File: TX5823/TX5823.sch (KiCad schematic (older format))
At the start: 73 parts, among them IC1 ATMEGA328P-A, IC2 ATTINY13A-SS, P1 Akku_in, P2 ISP, P3 Mavlink, Q3 MOSFET_N, SW1 SW_PUSH, SW2 SW_PUSH, U2 TPS54531, U3 TPS7A7200RGT, U4 CONN_03X08, U5 OPTO-TRANSISTOR4, U6 TX5823, U7 MAX7456_DS, U8 OPTO-TRANSISTOR4, X1 27MHz, Y1 16MHz

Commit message: an Layout gearbeitet
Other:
- note added: "Achtung, 5V nicht anschließen"
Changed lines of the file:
@@
 	9550 1500 9600 1500
 Connection ~ 9600 1100
+Text Notes 14500 8400 0    60   ~ 0
+Achtung, 5V nicht anschließen
 $EndSCHEMATC

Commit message: Layout fertig bis auf startup teil
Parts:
- D1: footprint (none) -> toni:POWERDI5
- U7: footprint toni:TSSOP-20_4.4x6.5mm_Pitch0.65mm_EP -> toni:TSSOP-28_4.4x9.7mm_Pitch0.65mm_EP
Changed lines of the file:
@@
 F 0 "U7" H 14400 6600 60  0000 C CNN
 F 1 "MAX7456_DS" H 14000 8050 60  0000 C CNN
-F 2 "toni:TSSOP-20_4.4x6.5mm_Pitch0.65mm_EP" H 13850 7200 60  0001 C CNN
+F 2 "toni:TSSOP-28_4.4x9.7mm_Pitch0.65mm_EP" H 13850 7200 60  0001 C CNN
 F 3 "" H 13850 7200 60  0000 C CNN
 	1    13850 7200
@@
 F 0 "D1" H 4500 8650 40  0000 C CNN
 F 1 "DIODE" H 4500 8450 40  0000 C CNN
-F 2 "" H 4500 8550 60  0001 C CNN
+F 2 "toni:POWERDI5" H 4500 8550 60  0001 C CNN
 F 3 "" H 4500 8550 60  0001 C CNN
 F 4 "PDS760-13" H 4500 8550 60  0001 C CNN "Teilenummer"

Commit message: zusätzlicher LDO für OSD hinzugefügt Softstart hinzugefügt
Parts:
- added C10: 220pF, Capacitors_SMD:C_0402, symbol C
- added C12, C4: 1uF, Capacitors_SMD:C_0603, symbol C
- added C13: 10uF, Capacitors_SMD:C_1206, symbol C
- added C6, C7: 100nF, Capacitors_SMD:C_0402, symbol C
- added C9: C, Capacitors_SMD:C_0603, symbol C
- added D2: ZENER, Diodes_SMD:Diode-MiniMELF_Standard, symbol ZENER
- added Q1: MOSFET_P, toni:SO8_WITH_EP, symbol MOSFET_P
- added R1, R2: R, Resistors_SMD:R_0603, symbol R
- added R3: R, Resistors_SMD:R_1206, symbol R
- added R4: 280k, Resistors_SMD:R_0603, symbol R
- added R5: 30,9k, Resistors_SMD:R_0603, symbol R
- added U1: TPS7A7200RGT, toni:QFN-16-1EP_3x3mm_Pitch0.5mm, symbol TPS7A7200RGT
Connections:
- net +5V: now also C10.1, C12.1, C13.1, R4.1, U1.15 (OUT), U1.16 (OUT); no longer C16.1, C17.1, C19.1, C21.1, L1.2, R10.1, R14.1, R25.1, U3.12 (EN), U3.13 (IN), U3.14 (IN), U4.14 (5_2), U4.17 (6_2)
- net Akku+: now also Q1.D, R3.1; no longer C1.1, C3.1, U2.2 (VIN)
- net GND: now also C12.2, C13.2, C4.2, C6.2, C7.2, R1.2, R5.2, U1.17 (EP), U1.7 (GND)
- new net: C7.1, U1.11 (SS)
- new net: C10.2, R4.2, R5.1, U1.2 (FB)
- new net: C9.1, D2.2 (K), Q1.G, R1.1, R2.1
- new net 5,2V: C16.1, C17.1, C19.1, C21.1, C4.1, C6.1, L1.2, R10.1, R14.1, R25.1, U1.12 (EN), U1.13 (IN), U1.14 (IN), U3.12 (EN), U3.13 (IN), U3.14 (IN), U4.14 (5_2), U4.17 (6_2)
- new net Akku+_SS: C1.1, C3.1, C9.2, D2.1 (A), Q1.S, R2.2, R3.2, U2.2 (VIN)
- no-connect marks 27 -> 35
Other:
- note added: "Softstart"
- note added: "TODO:\n12V Aufsteckplatine\nEingangsschutz"
- note removed: "TODO:\nEingangsfilterung (spule und diode)\n12V Aufsteckplatine"
- moved on the sheet: P1, P3, R26, R27, R28, SW2, U8

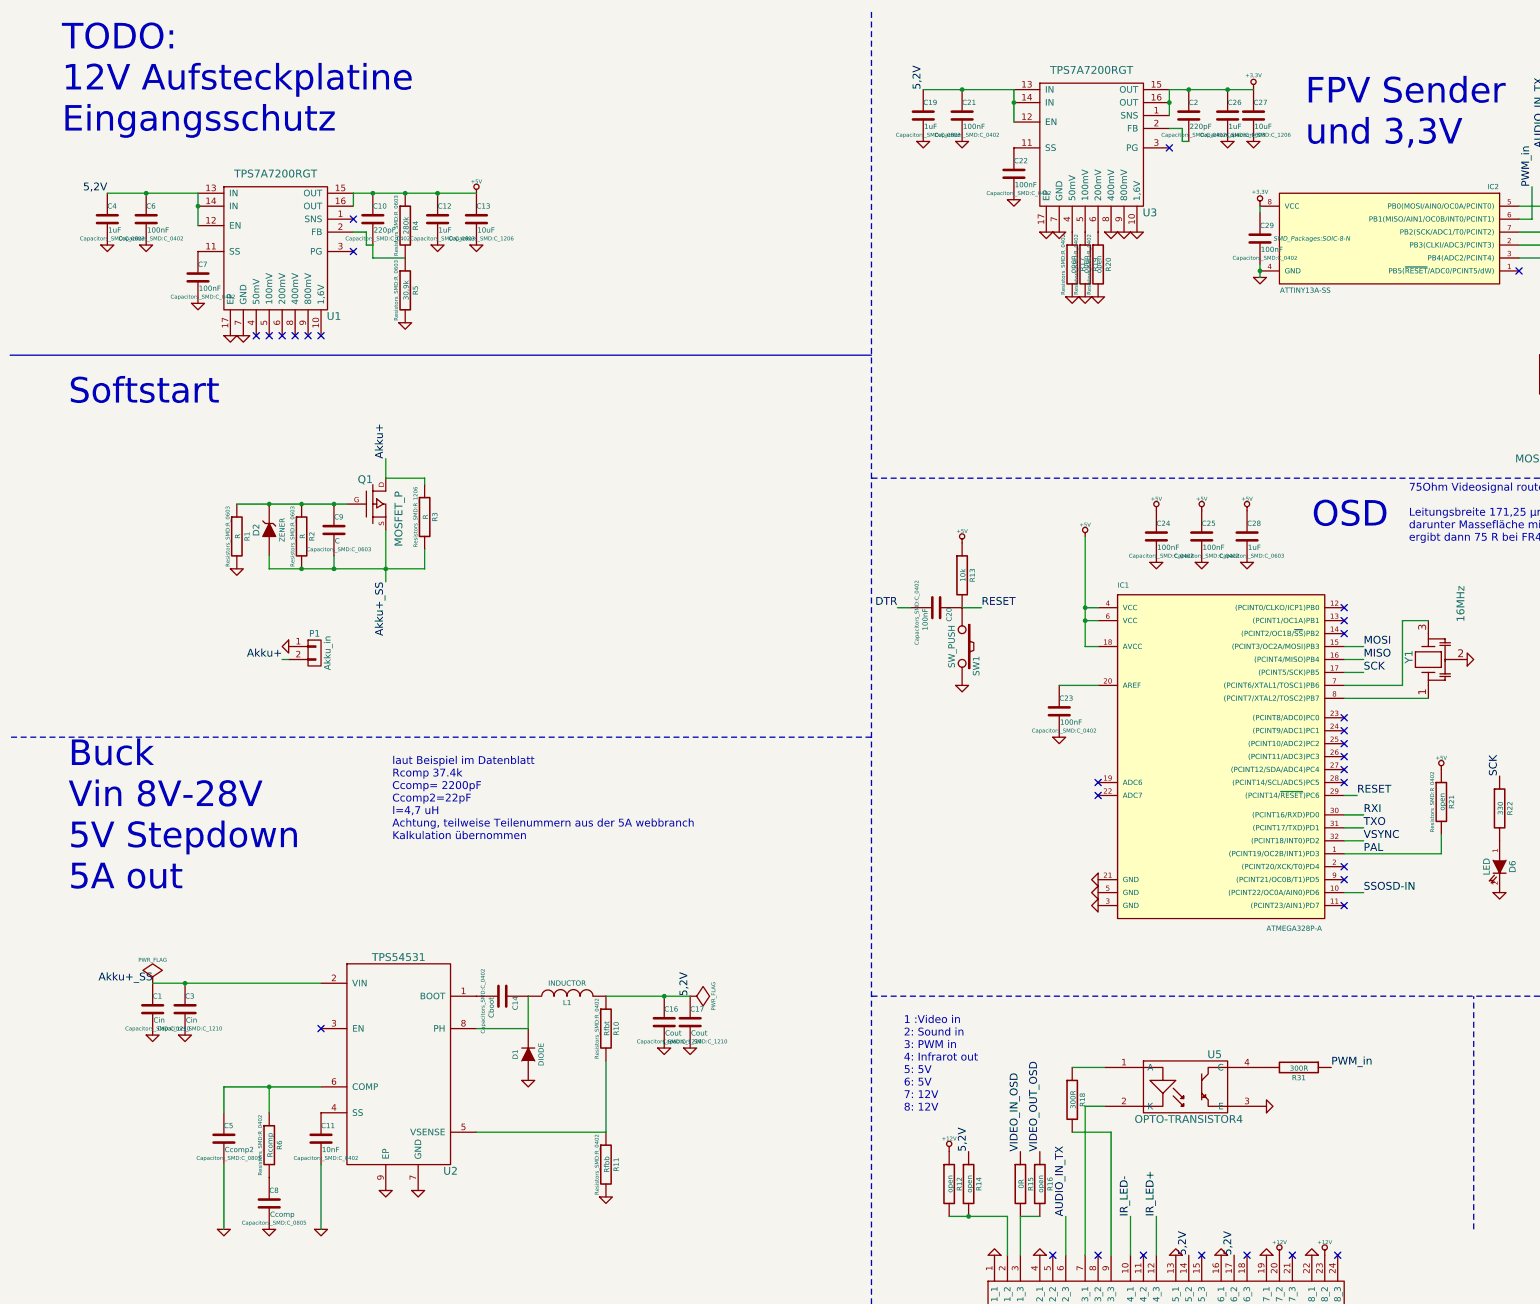
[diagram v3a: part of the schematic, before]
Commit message: Verbindungspunkte für 12V BuckBoost Aufsteckplatine hinzugefügt
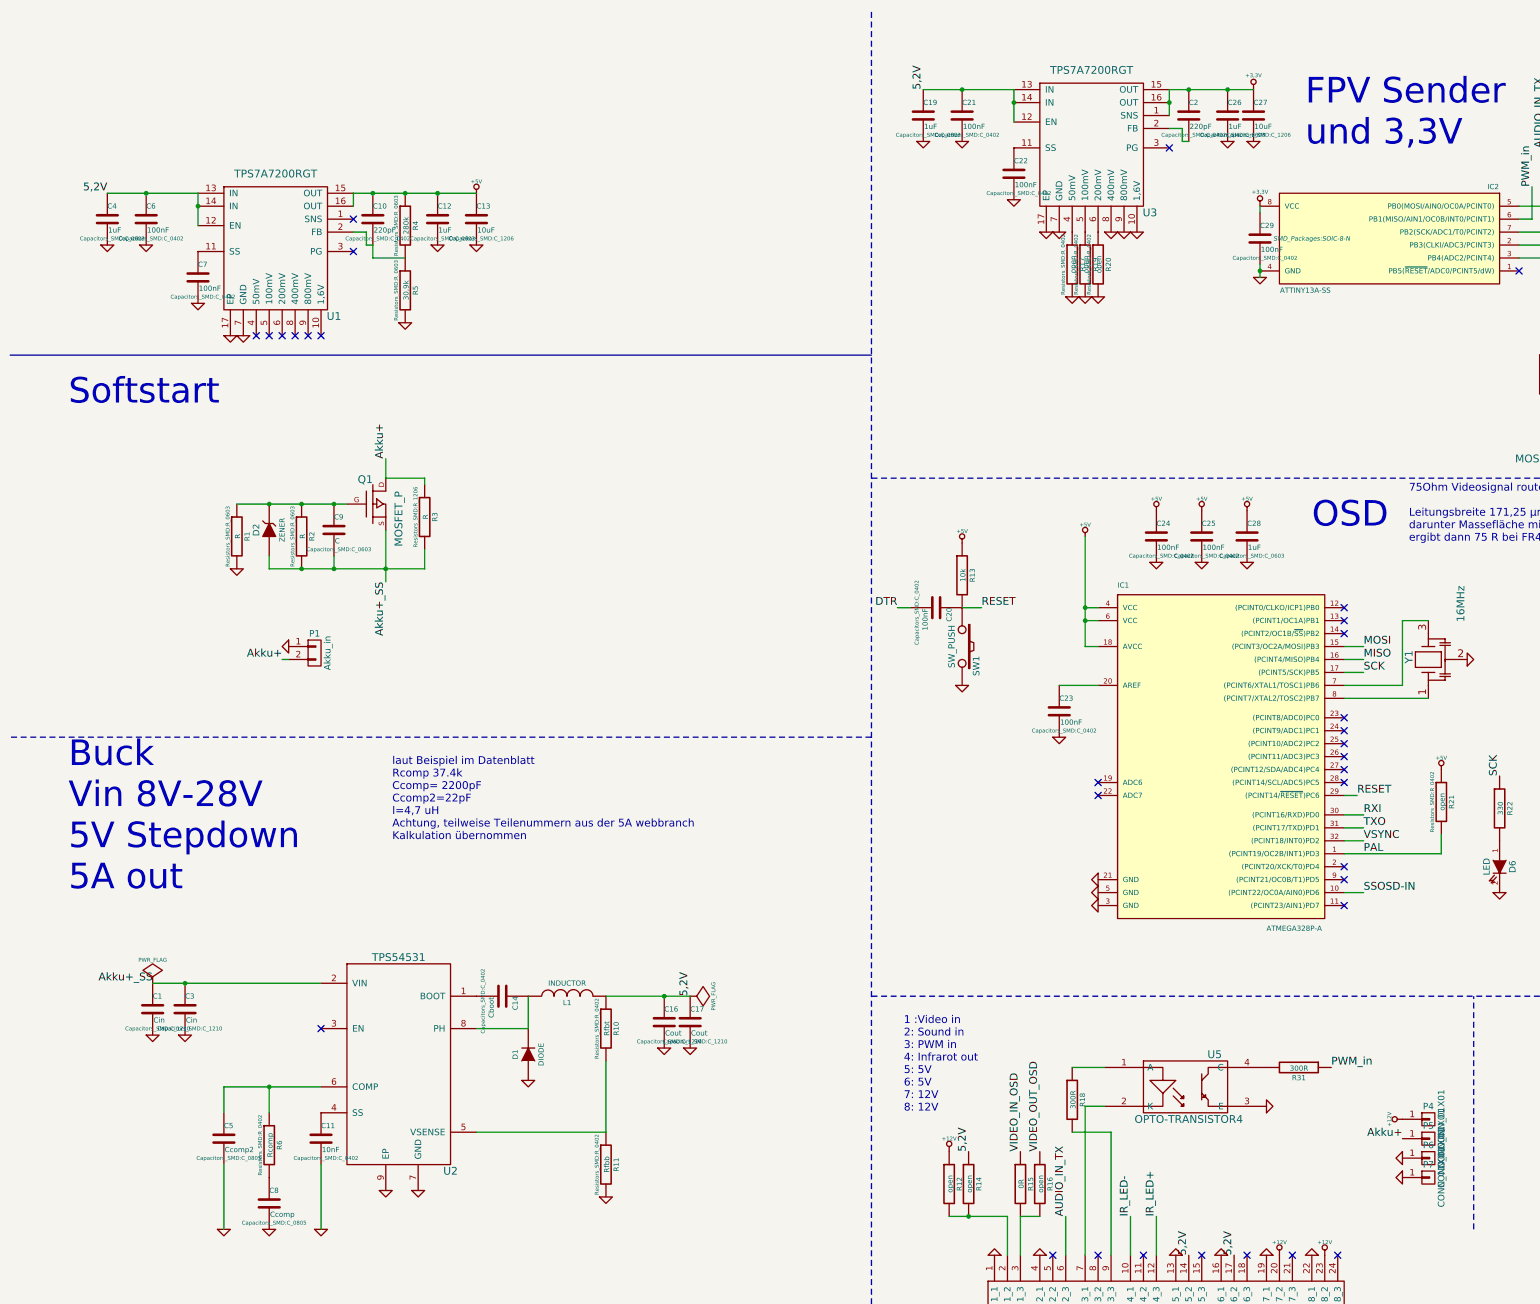
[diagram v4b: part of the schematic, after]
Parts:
- added P4, P5, P6, P7: CONN_01X01, Pin_Headers:Pin_Header_Straight_1x01, symbol CONN_01X01
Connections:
- net +12V: now also P4.1 (P1)
- net Akku+: now also P5.1 (P1)
- net GND: now also P6.1 (P1), P7.1 (P1)
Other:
- note removed: "TODO:\n12V Aufsteckplatine\nEingangsschutz"
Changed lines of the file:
@@
 	0    1    1    0
 $EndComp
-Text Notes 900  1450 0    197  ~ 0
-TODO:\n12V Aufsteckplatine\nEingangsschutz
 NoConn ~ 15300 5100
 NoConn ~ 15300 4700
@@
 Text Notes 950  3550 0    197  ~ 0
 Softstart
+$Comp
+L CONN_01X01 P4
+U 1 1 551FB334
+P 11450 9050
+F 0 "P4" H 11450 9150 50  0000 C CNN
+F 1 "CONN_01X01" V 11550 9050 50  0000 C CNN
+F 2 "Pin_Headers:Pin_Header_Straight_1x01" H 11450 9050 60  0001 C CNN
+F 3 "" H 11450 9050 60  0000 C CNN
+	1    11450 9050
+	1    0    0    -1
+$EndComp
+$Comp
+L CONN_01X01 P5
+U 1 1 551FB3E2
+P 11450 9200
+F 0 "P5" H 11450 9300 50  0000 C CNN
+F 1 "CONN_01X01" V 11550 9200 50  0000 C CNN
+F 2 "Pin_Headers:Pin_Header_Straight_1x01" H 11450 9200 60  0001 C CNN
+F 3 "" H 11450 9200 60  0000 C CNN
+	1    11450 9200
+	1    0    0    -1
+$EndComp
+$Comp
+L CONN_01X01 P6
+U 1 1 551FB45A
+P 11450 9350
+F 0 "P6" H 11450 9450 50  0000 C CNN
+F 1 "CONN_01X01" V 11550 9350 50  0000 C CNN
+F 2 "Pin_Headers:Pin_Header_Straight_1x01" H 11450 9350 60  0001 C CNN
+F 3 "" H 11450 9350 60  0000 C CNN
+	1    11450 9350
+	1    0    0    -1
+$EndComp
+$Comp
+L CONN_01X01 P7
+U 1 1 551FB4CB
+P 11450 9500
+F 0 "P7" H 11450 9600 50  0000 C CNN
+F 1 "CONN_01X01" V 11550 9500 50  0000 C CNN
+F 2 "Pin_Headers:Pin_Header_Straight_1x01" H 11450 9500 60  0001 C CNN
+F 3 "" H 11450 9500 60  0000 C CNN
+	1    11450 9500
+	1    0    0    -1
+$EndComp
+$Comp
+L +12V #PWR093
+U 1 1 551FB6C5
+P 11250 9050
+F 0 "#PWR093" H 11250 9000 20  0001 C CNN
+F 1 "+12V" H 11250 9150 30  0000 C CNN
+F 2 "" H 11250 9050 60  0000 C CNN
+F 3 "" H 11250 9050 60  0000 C CNN
+	1    11250 9050
+	0    -1   -1   0
+$EndComp
+Text Label 11250 9200 2    60   ~ 0
+Akku+
+$Comp
+L GND #PWR094
+U 1 1 551FBE5E
+P 11250 9350
+F 0 "#PWR094" H 11250 9350 30  0001 C CNN
+F 1 "GND" H 11250 9280 30  0001 C CNN
+F 2 "" H 11250 9350 60  0000 C CNN
+F 3 "" H 11250 9350 60  0000 C CNN
+	1    11250 9350
+	0    1    1    0
+$EndComp
+$Comp
+L GND #PWR095
+U 1 1 551FBEC5
+P 11250 9500
+F 0 "#PWR095" H 11250 9500 30  0001 C CNN
+F 1 "GND" H 11250 9430 30  0001 C CNN
+F 2 "" H 11250 9500 60  0000 C CNN
+F 3 "" H 11250 9500 60  0000 C CNN
+	1    11250 9500
+	0    1    1    0
+$EndComp
 $EndSCHEMATC

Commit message: DSBGA(&) Footprint für Löttests hinzugefügt. Keine relevanz für diese Platine
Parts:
- added U9: TPS22963, toni:DSBGS(6), symbol TPS22963
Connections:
- new net: U9.A1 (VOUT), U9.B1 (VOUT)
- new net: U9.A2 (VIN), U9.B2 (VIN)
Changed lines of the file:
@@
 	0    1    1    0
 $EndComp
+$Comp
+L TPS22963 U9
+U 1 1 551FFB80
+P 6000 2250
+F 0 "U9" H 6250 2050 60  0000 C CNN
+F 1 "TPS22963" H 6000 2900 60  0000 C CNN
+F 2 "toni:DSBGS(6)" H 6000 2250 60  0001 C CNN
+F 3 "" H 6000 2250 60  0000 C CNN
+	1    6000 2250
+	1    0    0    -1
+$EndComp
+Wire Wire Line
+	6500 1750 6500 1850
+Wire Wire Line
+	5550 1750 5550 1850
 $EndSCHEMATC

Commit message: letzte Änderungen für Fertigung Gerberdaten hinzugefügt
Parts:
- Q1: Teilenummer (none) -> FDS6982AS
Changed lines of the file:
@@
 F 2 "toni:SO8_WITH_EP" H 3300 4300 60  0001 C CNN
 F 3 "" H 3300 4300 60  0000 C CNN
+F 4 "FDS6982AS" H 3300 4300 60  0001 C CNN "Teilenummer"
 	1    3300 4300
 	1    0    0    -1

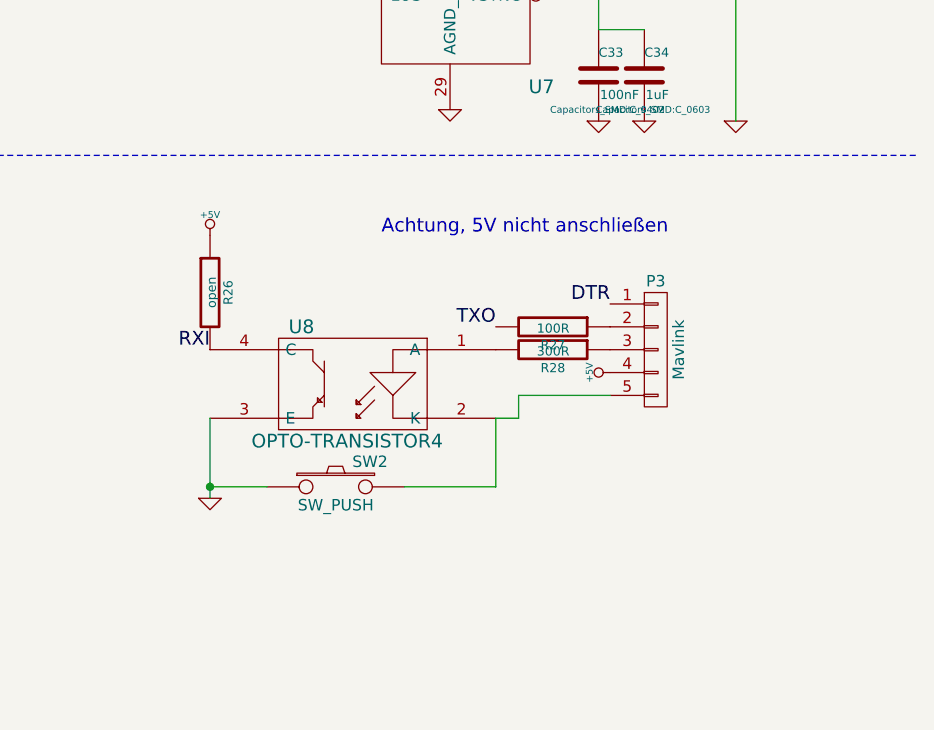
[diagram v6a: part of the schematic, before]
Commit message: mavlink isolierung überarbeitet. adum hinzugefüt
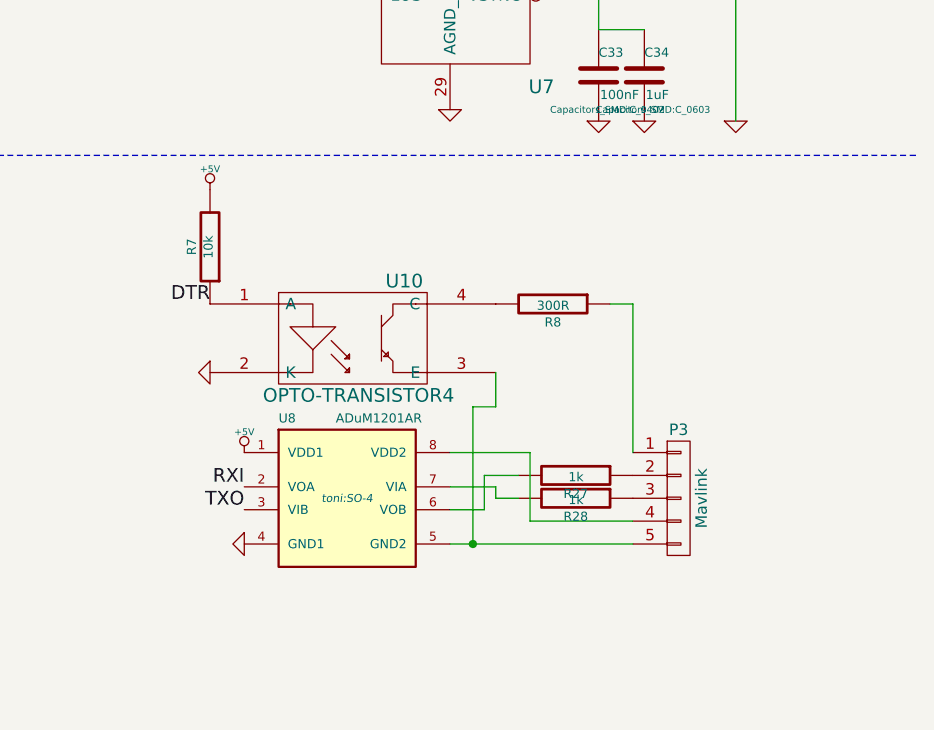
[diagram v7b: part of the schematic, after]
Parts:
- removed R26: open, Resistors_SMD:R_0603, symbol R
- removed SW2: SW_PUSH, toni:EVQP7A, symbol SW_PUSH
- removed U8: OPTO-TRANSISTOR4, toni:SO-4, symbol OPTO-TRANSISTOR4
- added R7: 10k, Resistors_SMD:R_0603, symbol R
- added R8: 300R, Resistors_SMD:R_0603, symbol R
- added U10: OPTO-TRANSISTOR4, toni:SO-4, symbol OPTO-TRANSISTOR4
- added U8: ADuM1201AR, toni:SO-4, symbol ADuM1201AR
- R27: value 100R -> 1k
- R28: value 300R -> 1k
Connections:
- net +5V: now also R7.2, U8.1 (VDD1); no longer P3.4 (P4)
- net DTR: now also R7.1, U10.1 (A); no longer P3.1 (P1)
- net GND: now also U10.2 (K), U8.4 (GND1)
- net RXI: now also U8.2 (VOA)
- net TXO: now also U8.3 (VIB); no longer R27.2
- net at P3.5 (P5): now also U10.3 (E), U8.5 (GND2)
- net at R28.2: now also U8.7 (VIA)
- new net: P3.1 (P1), R8.1
- new net: P3.4 (P4), U8.8 (VDD2)
- new net: R27.2, U8.6 (VOB)
- new net: R8.2, U10.4 (C)
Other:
- note removed: "Achtung, 5V nicht anschließen"
- moved on the sheet: P3, R27, R28

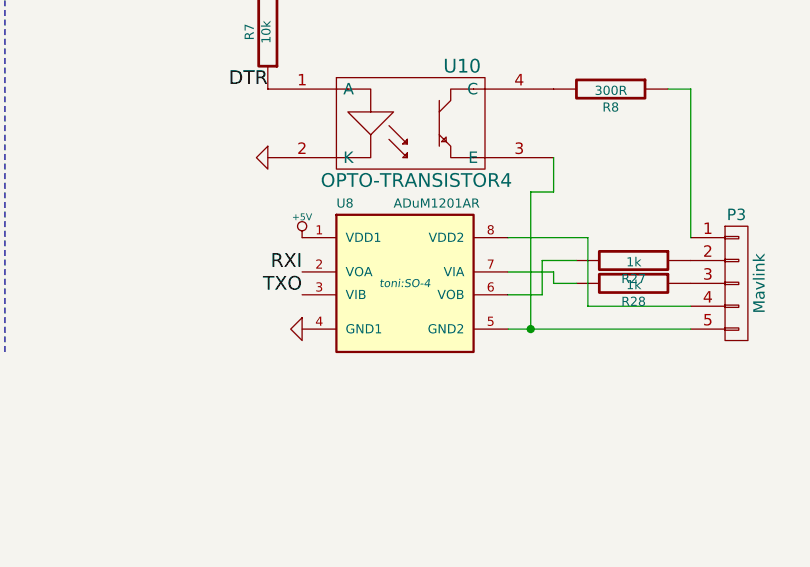
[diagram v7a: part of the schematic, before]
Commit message: footprint adum angepasst
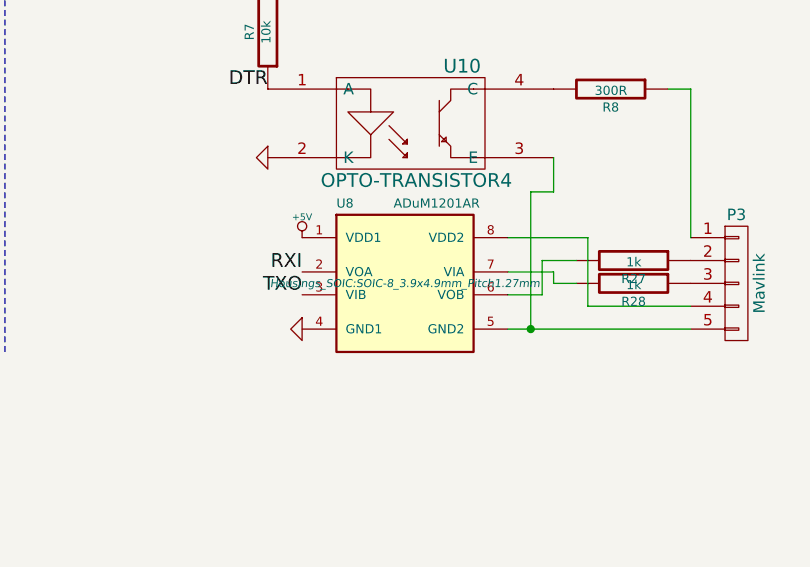
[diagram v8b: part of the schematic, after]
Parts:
- U8: footprint toni:SO-4 -> Housings_SOIC:SOIC-8_3.9x4.9mm_Pitch1.27mm
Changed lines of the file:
@@
 F 0 "U8" H 13250 9950 40  0000 L CNN
 F 1 "ADuM1201AR" H 13500 9950 40  0000 L CNN
-F 2 "toni:SO-4" H 13550 9600 35  0000 C CIN
+F 2 "Housings_SOIC:SOIC-8_3.9x4.9mm_Pitch1.27mm" H 13550 9600 35  0000 C CIN
 F 3 "" H 13550 9600 60  0000 C CNN
 	1    13550 9600
